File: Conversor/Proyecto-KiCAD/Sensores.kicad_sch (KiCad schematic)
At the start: 25 parts, among them U10 OPA365xxD, U7 TMCS1100A4, U8 LM5056APMH/NOPB, U9 ISO7242C

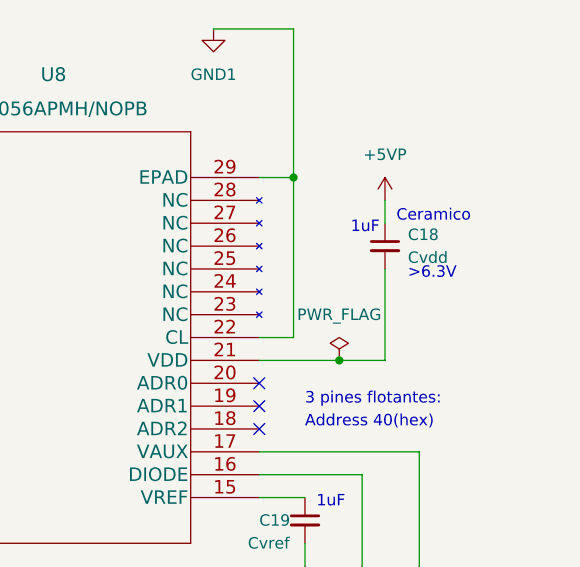
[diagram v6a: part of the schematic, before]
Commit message: Continuar con el diseño de la PCB
- Agregar los agujeros de tornillos
- Terminar la parte del secundario
- Agregar el borde en Egde.cuts que causaba problema
- Corregir las pista que no entran derechas a los pads
- Cambiar las footprints de los conectores
Por hacer:
  - Consultar de componentes como headers a Claus
  - Una vez terminada pedir cotización en las paginas que me pasó Jorge (Bookmarks de Firefox)
  - Ver de agrear un selector para la alimentación externa por header en la entrada de 12-18V (preguntar a Claus)
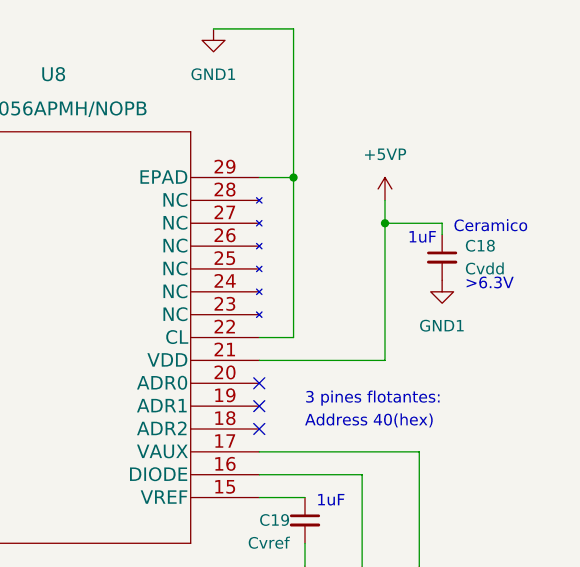
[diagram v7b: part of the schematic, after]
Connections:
- net +5VP: now also U8.21 (VDD)
- net GND1: now also C18.2
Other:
- moved on the sheet: C18
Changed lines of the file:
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@@
   (junction (at 104.14 109.22) (diameter 0) (color 0 0 0 0)
   )
-  (junction (at 261.62 57.15) (diameter 0) (color 0 0 0 0)
-  )
   (junction (at 196.85 59.69) (diameter 0) (color 0 0 0 0)
   )
   (junction (at 213.36 140.97) (diameter 0) (color 0 0 0 0)
+  )
+  (junction (at 266.7 41.91) (diameter 0) (color 0 0 0 0)
   )
   (junction (at 142.24 40.64) (diameter 0) (color 0 0 0 0)
@@
     (stroke (width 0) (type default) (color 0 0 0 0))
   )
+  (wire (pts (xy 148.59 64.77) (xy 128.27 64.77))
+    (stroke (width 0) (type default) (color 0 0 0 0))
+  )
+  (wire (pts (xy 138.43 50.8) (xy 138.43 53.34))
+    (stroke (width 0) (type default) (color 0 0 0 0))
+  )
+  (wire (pts (xy 245.11 125.73) (xy 245.11 138.43))
+    (stroke (width 0) (type default) (color 0 0 0 0))
+  )
+  (wire (pts (xy 245.11 125.73) (xy 238.76 125.73))
+    (stroke (width 0) (type default) (color 0 0 0 0))
+  )
+  (wire (pts (xy 238.76 125.73) (xy 238.76 97.79))
+    (stroke (width 0) (type default) (color 0 0 0 0))
+  )
+  (wire (pts (xy 104.14 109.22) (xy 104.14 110.49))
+    (stroke (width 0) (type default) (color 0 0 0 0))
+  )
+  (wire (pts (xy 264.16 69.85) (xy 252.73 69.85))
+    (stroke (width 0) (type default) (color 0 0 0 0))
+  )
+  (wire (pts (xy 43.18 64.77) (xy 43.18 90.17))
+    (stroke (width 0) (type default) (color 0 0 0 0))
+  )
+  (wire (pts (xy 171.45 41.91) (xy 171.45 95.25))
+    (stroke (width 0) (type default) (color 0 0 0 0))
+  )
+  (wire (pts (xy 236.22 133.35) (xy 236.22 135.89))
+    (stroke (width 0) (type default) (color 0 0 0 0))
+  )
+  (wire (pts (xy 142.24 40.64) (xy 134.62 40.64))
+    (stroke (width 0) (type default) (color 0 0 0 0))
+  )
+  (wire (pts (xy 57.15 110.49) (xy 57.15 115.57))
+    (stroke (width 0) (type default) (color 0 0 0 0))
+  )
+  (wire (pts (xy 154.94 52.07) (xy 154.94 67.31))
+    (stroke (width 0) (type default) (color 0 0 0 0))
+  )
+  (wire (pts (xy 252.73 54.61) (xy 256.54 54.61))
+    (stroke (width 0) (type default) (color 0 0 0 0))
+  )
+  (wire (pts (xy 199.39 121.92) (xy 199.39 120.65))
+    (stroke (width 0) (type default) (color 0 0 0 0))
+  )
+  (wire (pts (xy 102.87 50.8) (xy 95.25 50.8))
+    (stroke (width 0) (type default) (color 0 0 0 0))
+  )
   (wire (pts (xy 266.7 39.37) (xy 266.7 41.91))
-    (stroke (width 0) (type default) (color 0 0 0 0))
-  )
-  (wire (pts (xy 148.59 64.77) (xy 128.27 64.77))
-    (stroke (width 0) (type default) (color 0 0 0 0))
-  )
-  (wire (pts (xy 138.43 50.8) (xy 138.43 53.34))
-    (stroke (width 0) (type default) (color 0 0 0 0))
-  )
-  (wire (pts (xy 245.11 125.73) (xy 245.11 138.43))
-    (stroke (width 0) (type default) (color 0 0 0 0))
-  )
-  (wire (pts (xy 245.11 125.73) (xy 238.76 125.73))
-    (stroke (width 0) (type default) (color 0 0 0 0))
-  )
-  (wire (pts (xy 238.76 125.73) (xy 238.76 97.79))
-    (stroke (width 0) (type default) (color 0 0 0 0))
-  )
-  (wire (pts (xy 104.14 109.22) (xy 104.14 110.49))
-    (stroke (width 0) (type default) (color 0 0 0 0))
-  )
-  (wire (pts (xy 264.16 69.85) (xy 252.73 69.85))
-    (stroke (width 0) (type default) (color 0 0 0 0))
-  )
-  (wire (pts (xy 43.18 64.77) (xy 43.18 90.17))
-    (stroke (width 0) (type default) (color 0 0 0 0))
-  )
-  (wire (pts (xy 171.45 41.91) (xy 171.45 95.25))
-    (stroke (width 0) (type default) (color 0 0 0 0))
-  )
-  (wire (pts (xy 236.22 133.35) (xy 236.22 135.89))
-    (stroke (width 0) (type default) (color 0 0 0 0))
-  )
-  (wire (pts (xy 142.24 40.64) (xy 134.62 40.64))
-    (stroke (width 0) (type default) (color 0 0 0 0))
-  )
-  (wire (pts (xy 57.15 110.49) (xy 57.15 115.57))
-    (stroke (width 0) (type default) (color 0 0 0 0))
-  )
-  (wire (pts (xy 154.94 52.07) (xy 154.94 67.31))
-    (stroke (width 0) (type default) (color 0 0 0 0))
-  )
-  (wire (pts (xy 252.73 54.61) (xy 256.54 54.61))
-    (stroke (width 0) (type default) (color 0 0 0 0))
-  )
-  (wire (pts (xy 199.39 121.92) (xy 199.39 120.65))
-    (stroke (width 0) (type default) (color 0 0 0 0))
-  )
-  (wire (pts (xy 102.87 50.8) (xy 95.25 50.8))
-    (stroke (width 0) (type default) (color 0 0 0 0))
-  )
-  (wire (pts (xy 266.7 57.15) (xy 266.7 46.99))
     (stroke (width 0) (type default) (color 0 0 0 0))
   )
@@
     (stroke (width 0) (type default) (color 0 0 0 0))
   )
+  (wire (pts (xy 273.05 43.18) (xy 273.05 41.91))
+    (stroke (width 0) (type default) (color 0 0 0 0))
+  )
   (wire (pts (xy 104.14 54.61) (xy 105.41 54.61))
     (stroke (width 0) (type default) (color 0 0 0 0))
@@
     (stroke (width 0) (type default) (color 0 0 0 0))
   )
-  (wire (pts (xy 261.62 57.15) (xy 252.73 57.15))
+  (wire (pts (xy 252.73 57.15) (xy 266.7 57.15))
     (stroke (width 0) (type default) (color 0 0 0 0))
   )
@@
     (stroke (width 0) (type default) (color 0 0 0 0))
   )
+  (wire (pts (xy 273.05 41.91) (xy 266.7 41.91))
+    (stroke (width 0) (type default) (color 0 0 0 0))
+  )
   (wire (pts (xy 148.59 40.64) (xy 154.94 40.64))
     (stroke (width 0) (type default) (color 0 0 0 0))
@@
     (stroke (width 0) (type default) (color 0 0 0 0))
   )
-  (wire (pts (xy 261.62 57.15) (xy 266.7 57.15))
-    (stroke (width 0) (type default) (color 0 0 0 0))
-  )
   (wire (pts (xy 83.82 156.21) (xy 76.2 156.21))
     (stroke (width 0) (type default) (color 0 0 0 0))
@@
   )
   (wire (pts (xy 205.74 120.65) (xy 205.74 133.35))
+    (stroke (width 0) (type default) (color 0 0 0 0))
+  )
+  (wire (pts (xy 266.7 41.91) (xy 266.7 57.15))
     (stroke (width 0) (type default) (color 0 0 0 0))
   )
@@
     (effects (font (size 1.27 1.27)) (justify left bottom))
   )
-  (text ">6.3V" (at 269.24 48.26 0)
+  (text ">6.3V" (at 275.59 49.53 0)
     (effects (font (size 1.27 1.27)) (justify left bottom))
   )
@@
     (effects (font (size 2.54 2.54) bold) (justify left bottom))
   )
-  (text "Ceramico" (at 267.97 41.91 0)
+  (text "Ceramico" (at 274.32 43.18 0)
     (effects (font (size 1.27 1.27)) (justify left bottom))
   )
@@
     (effects (font (size 2.54 2.54) (thickness 0.508) bold) (justify left bottom))
   )
-  (text "1uF" (at 262.89 43.18 0)
+  (text "1uF" (at 269.24 44.45 0)
     (effects (font (size 1.27 1.27)) (justify left bottom))
   )
@@
     (pin "2")
   )
-  (symbol (lib_id "power:PWR_FLAG") (at 261.62 57.15 0) (mirror y) (unit 1)
-    (in_bom yes) (on_board yes) (fields_autoplaced)
-    (property "Reference" "#FLG0102" (id 0) (at 261.62 55.245 0)
-      (effects (font (size 1.27 1.27)) hide)
-    )
-    (property "Value" "PWR_FLAG" (id 1) (at 261.62 52.07 0))
-    (property "Footprint" "" (id 2) (at 261.62 57.15 0)
-      (effects (font (size 1.27 1.27)) hide)
-    )
-    (property "Datasheet" "~" (id 3) (at 261.62 57.15 0)
-      (effects (font (size 1.27 1.27)) hide)
-    )
-    (pin "1")
-  )
   (symbol (lib_id "power:+3V3") (at 57.15 110.49 0) (unit 1)
     (in_bom yes) (on_board yes) (fields_autoplaced)
@@
     )
     (property "Datasheet" "" (id 3) (at 102.87 73.66 0)
+      (effects (font (size 1.27 1.27)) hide)
+    )
+    (pin "1")
+  )
+  (symbol (lib_id "power:GND1") (at 273.05 48.26 0) (unit 1)
+    (in_bom yes) (on_board yes) (fields_autoplaced)
+    (property "Reference" "#PWR0146" (id 0) (at 273.05 54.61 0)
+      (effects (font (size 1.27 1.27)) hide)
+    )
+    (property "Value" "GND1" (id 1) (at 273.05 53.34 0))
+    (property "Footprint" "" (id 2) (at 273.05 48.26 0)
+      (effects (font (size 1.27 1.27)) hide)
+    )
+    (property "Datasheet" "" (id 3) (at 273.05 48.26 0)
       (effects (font (size 1.27 1.27)) hide)
     )
@@
     (pin "2")
   )
-  (symbol (lib_id "Device:C_Small") (at 266.7 44.45 0) (unit 1)
-    (in_bom yes) (on_board yes)
-    (property "Reference" "C18" (id 0) (at 269.24 43.1862 0)
-      (effects (font (size 1.27 1.27)) (justify left))
-    )
-    (property "Value" "Cvdd" (id 1) (at 269.24 45.7262 0)
-      (effects (font (size 1.27 1.27)) (justify left))
-    )
-    (property "Footprint" "Capacitor_SMD:C_1206_3216Metric_Pad1.33x1.80mm_HandSolder" (id 2) (at 266.7 44.45 0)
-      (effects (font (size 1.27 1.27)) hide)
-    )
-    (property "Datasheet" "~" (id 3) (at 266.7 44.45 0)
-      (effects (font (size 1.27 1.27)) hide)
-    )
+  (symbol (lib_id "Device:C_Small") (at 273.05 45.72 0) (unit 1)
+    (in_bom yes) (on_board yes)
+    (property "Reference" "C18" (id 0) (at 275.59 44.4562 0)
+      (effects (font (size 1.27 1.27)) (justify left))
+    )
+    (property "Value" "Cvdd" (id 1) (at 275.59 46.9962 0)
+      (effects (font (size 1.27 1.27)) (justify left))
+    )
+    (property "Footprint" "Capacitor_SMD:C_1206_3216Metric_Pad1.33x1.80mm_HandSolder" (id 2) (at 273.05 45.72 0)
+      (effects (font (size 1.27 1.27)) hide)
+    )
+    (property "Datasheet" "~" (id 3) (at 273.05 45.72 0)
+      (effects (font (size 1.27 1.27)) hide)
+    )
